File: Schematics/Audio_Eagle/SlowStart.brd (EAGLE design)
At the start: 100 x 80 mm, 19 parts

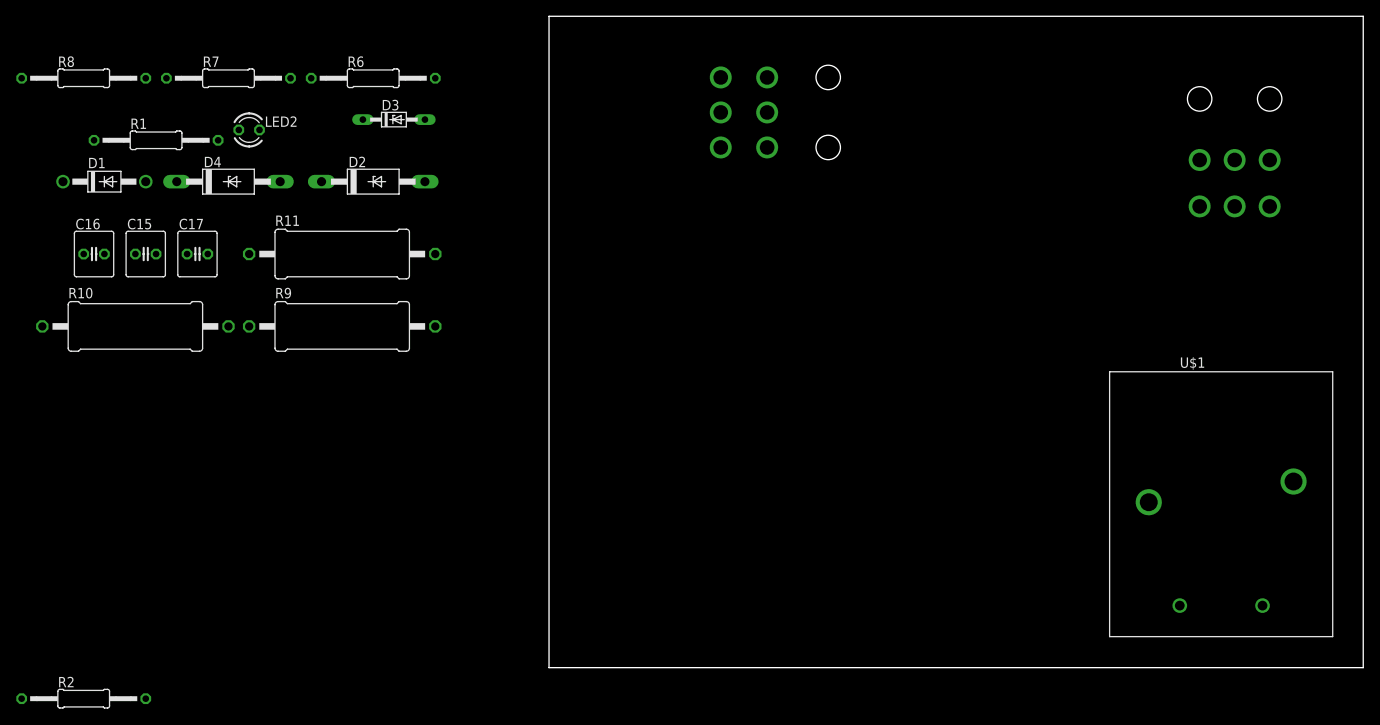
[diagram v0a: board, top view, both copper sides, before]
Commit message: updated slow start
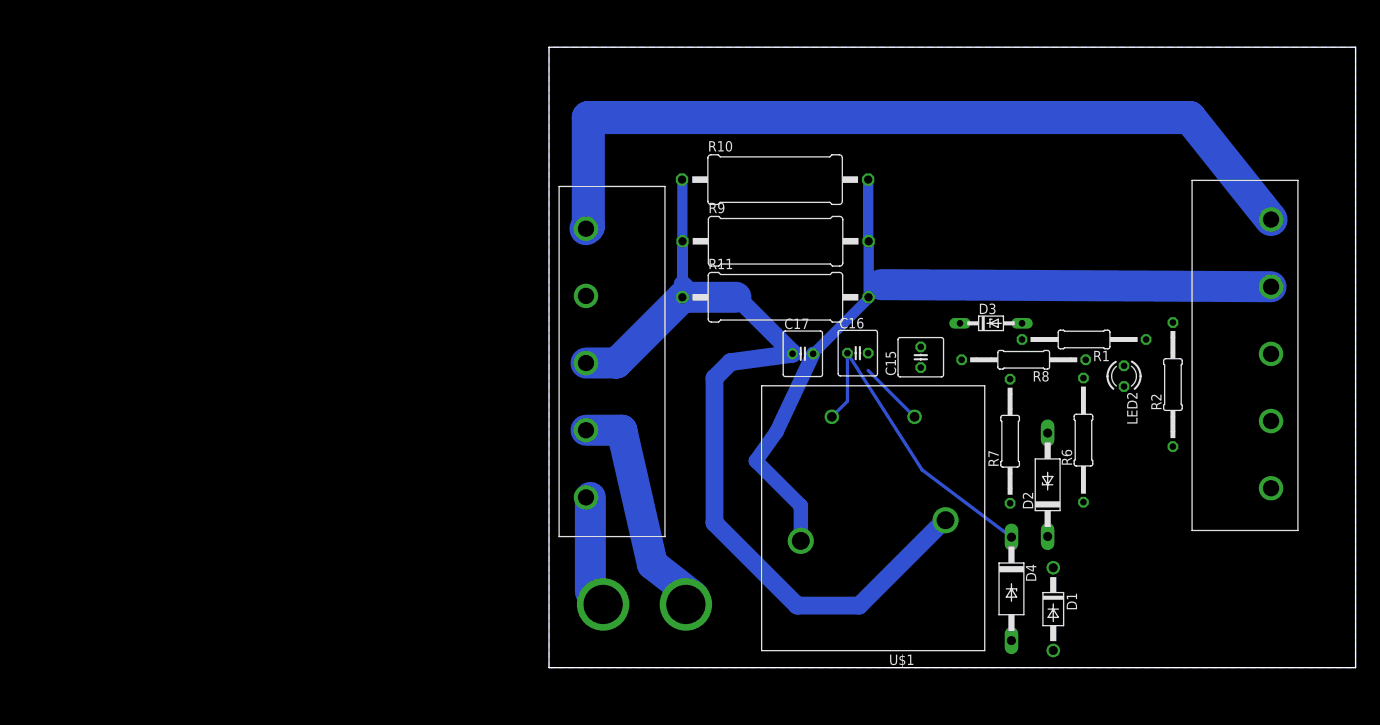
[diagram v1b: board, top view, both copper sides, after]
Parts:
- added U$4: FUSE, Amplifier_Parts:FUSE_PADS
- U$2, U$3: value MOLEX_6P -> SCREW_TERMINAL_5; device Amplifier_Parts:MOLEX_6P -> Amplifier_Parts:SCREW_TERMINAL_5
- moved R2 139.2 mm to (76.6, 34.8), turned to 90 degrees
- moved D1 127.8 mm to (61.9, 7.19), turned to 270 degrees
- moved R8 120.5 mm to (58.3, 37.8), turned to 180 degrees
- moved R1 116.6 mm to (65.7, 40.3), turned to 180 degrees
- moved LED2 111.6 mm to (70.6, 35.8), turned to 270 degrees
- moved D4 108.4 mm to (56.8, 9.68), turned to 270 degrees
- moved R7 105.8 mm to (56.6, 27.8), turned to 90 degrees
- moved R6 97.9 mm to (65.6, 27.9), turned to 90 degrees
- moved C15 96.0 mm to (45.7, 38.1), turned to 90 degrees
- moved C16 94.6 mm to (37.9, 38.6)
- moved D2 90.8 mm to (61.2, 22.5), turned to 90 degrees
- moved U$2 88.0 mm to (2.54, 38.1), turned to 270 degrees
- moved R10 80.6 mm to (27.8, 59.9)
- moved D3 77.5 mm to (54.3, 42.3)
- moved C17 75.4 mm to (31.2, 38.5)
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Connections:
- removed net N$1 (its old number): U$2.P$3, U$2.P$4
- new net VAC+: U$2.P$4, U$3.P$6
- new net VAC-: C17.1, R10.1, R11.1, R9.1, U$1.COM, U$2.P$3
- net GND: now also U$2.P$2; no longer U$2.P$1
- net N$12: now also U$3.P$4; no longer U$3.P$5
- net N$2: now also U$2.P$6, U$4.P$2; no longer U$2.P$5, U$3.P$3
- net N$3: now also R2.2, U$3.P$3; no longer C17.1, R10.1, R11.1, R9.1, U$1.COM, U$2.P$2
- net N$5: now also U$2.P$5, U$4.P$1; no longer R2.2, U$3.P$2
- net N$8: now also U$3.P$5; no longer U$3.P$4
- net VCC: no longer U$3.P$1
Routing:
- net VAC-: track 0.00 -> 133.6 mm
- net VAC+: track 0.00 -> 103.7 mm
- net N$8: track 0.00 -> 101.4 mm
- net N$10: track 0.00 -> 39.4 mm
- net N$5: track 0.00 -> 29.1 mm
- net N$2: track 0.00 -> 14.3 mm
- net GND: track 0.00 -> 8.06 mm
- added copper zone on layer 16, net GND
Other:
- board size 100 x 80 mm -> 99.1 x 76.2 mm

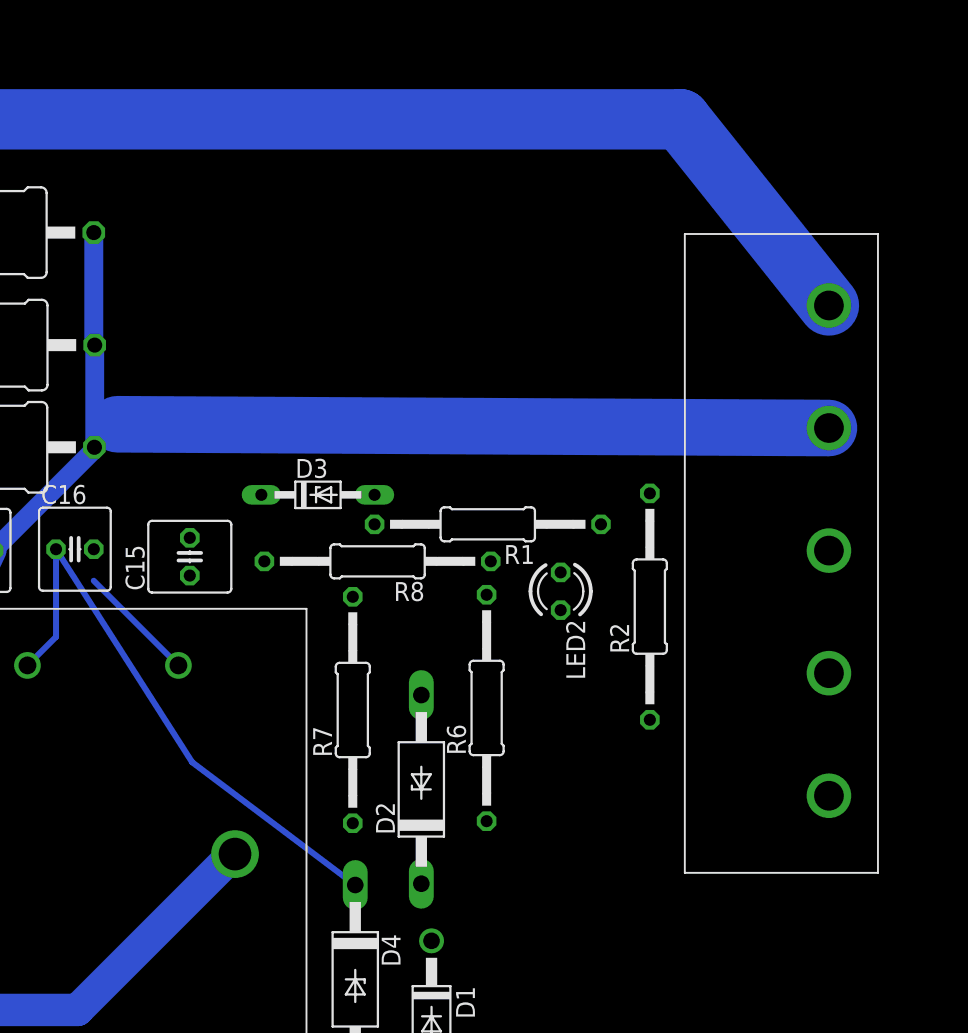
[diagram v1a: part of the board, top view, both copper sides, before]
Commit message: updated to slow start board
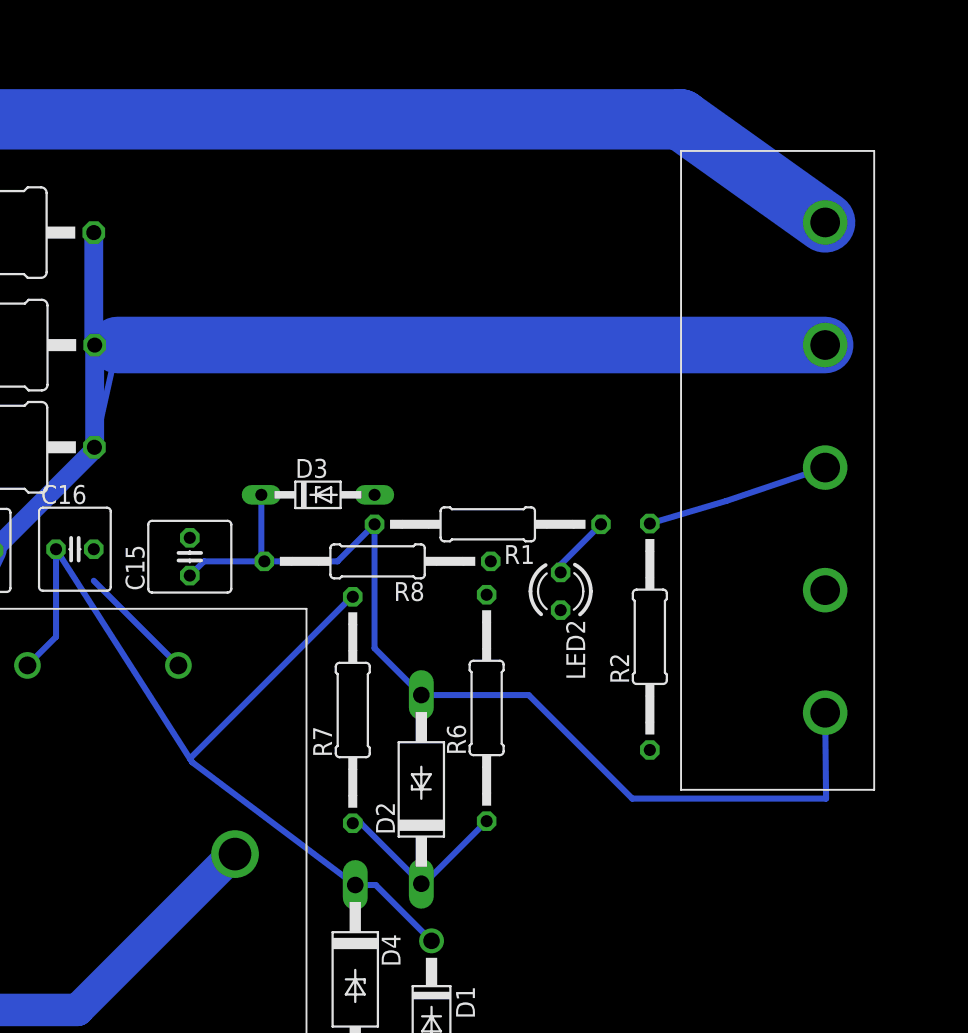
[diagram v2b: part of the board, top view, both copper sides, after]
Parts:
- moved U$3 5.59 mm to (90.4, 43.4)
- moved R2 2.03 mm to (76.6, 32.7)
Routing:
- net N$12: track 0.00 -> 67.1 mm
- net N$10: track 39.4 -> 61.5 mm
- net N$11: track 0.00 -> 12.4 mm
- net N$3: track 0.00 -> 12.4 mm
- net N$8: track 101.4 -> 106.0 mm
- net N$1: track 0.00 -> 4.36 mm
- net VAC+: track 103.7 -> 99.6 mm
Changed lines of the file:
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@@
 </element>
 <element name="R1" library="resistor" package="0207/15" value="10k" x="65.7141" y="40.3049625" rot="R180"/>
-<element name="R2" library="resistor" package="0207/15" value="100" x="76.623821875" y="34.768103125" rot="R90"/>
+<element name="R2" library="resistor" package="0207/15" value="100" x="76.623821875" y="32.736103125" rot="R90"/>
 <element name="U$4" library="Amplifier_Parts" package="FUSE_PADS" value="FUSE" x="11.7266" y="7.763428125" rot="R180"/>
 <element name="U$2" library="Amplifier_Parts" package="SCREW_TERMINAL_5" value="SCREW_TERMINAL_5" x="2.54" y="38.1" rot="R270"/>
-<element name="U$3" library="Amplifier_Parts" package="SCREW_TERMINAL_5" value="SCREW_TERMINAL_5" x="90.678" y="37.846" rot="R90"/>
+<element name="U$3" library="Amplifier_Parts" package="SCREW_TERMINAL_5" value="SCREW_TERMINAL_5" x="90.424" y="43.434" rot="R90"/>
 </elements>
 <signals>
@@
 <wire x1="39.23845" y1="45.489928125" x2="39.23845" y2="45.34414375" width="1.27" layer="16"/>
 <wire x1="39.23845" y1="45.34414375" x2="32.4429" y2="38.54859375" width="1.27" layer="16"/>
-<wire x1="39.257265625" y1="45.50874375" x2="40.788521875" y2="47.04" width="0.4064" layer="16"/>
-<wire x1="40.788521875" y1="47.04" x2="88.678" y2="46.786" width="3.81" layer="16"/>
+<wire x1="39.257265625" y1="45.50874375" x2="40.788521875" y2="52.374" width="0.4064" layer="16"/>
+<wire x1="40.788521875" y1="52.374" x2="88.424" y2="52.374" width="3.81" layer="16"/>
 </signal>
 <signal name="N$10">
@@
 <wire x1="56.795371875" y1="16.027840625" x2="45.820628125" y2="24.288884375" width="0.4064" layer="16"/>
 <wire x1="45.820628125" y1="24.288884375" x2="36.65525625" y2="38.629" width="0.4064" layer="16"/>
-<wire x1="45.820628125" y1="24.288884375" x2="56.6285875" y2="35.426621875" width="0" layer="19" extent="16-16"/>
-<wire x1="61.9296125" y1="12.269978125" x2="56.795371875" y2="16.027840625" width="0" layer="19" extent="1-1"/>
+<wire x1="56.6285875" y1="35.426621875" x2="56.55949375" y2="35.426621875" width="0.4064" layer="16"/>
+<wire x1="56.55949375" y1="35.426621875" x2="45.665096875" y2="24.532225" width="0.4064" layer="16"/>
+<wire x1="56.795371875" y1="16.027840625" x2="58.17175" y2="16.027840625" width="0.4064" layer="16"/>
+<wire x1="58.17175" y1="16.027840625" x2="61.9296125" y2="12.269978125" width="0.4064" layer="16"/>
+<wire x1="45.820628125" y1="24.288884375" x2="45.665096875" y2="24.532225" width="0" layer="19" extent="16-16"/>
 </signal>
 <signal name="N$11">
@@
 <contactref element="R6" pad="1"/>
 <contactref element="D2" pad="C"/>
-<wire x1="61.242603125" y1="16.113271875" x2="65.637840625" y2="20.324825" width="0" layer="19" extent="1-1"/>
-<wire x1="56.6285875" y1="20.186621875" x2="61.242603125" y2="16.113271875" width="0" layer="19" extent="1-1"/>
+<wire x1="56.6285875" y1="20.186621875" x2="57.169253125" y2="20.186621875" width="0.4064" layer="16"/>
+<wire x1="57.169253125" y1="20.186621875" x2="61.242603125" y2="16.113271875" width="0.4064" layer="16"/>
+<wire x1="61.242603125" y1="16.113271875" x2="61.4262875" y2="16.113271875" width="0.4064" layer="16"/>
+<wire x1="61.4262875" y1="16.113271875" x2="65.637840625" y2="20.324825" width="0.4064" layer="16"/>
 </signal>
 <signal name="N$12">
@@
 <contactref element="R1" pad="2"/>
 <contactref element="U$3" pad="P$4"/>
-<wire x1="61.242603125" y1="28.813271875" x2="88.678" y2="22.036" width="0" layer="19" extent="1-1"/>
-<wire x1="58.0941" y1="40.3049625" x2="61.242603125" y2="28.813271875" width="0" layer="19" extent="1-1"/>
-<wire x1="50.677503125" y1="37.812834375" x2="58.0941" y2="40.3049625" width="0" layer="19" extent="1-1"/>
-<wire x1="50.47415" y1="42.289403125" x2="50.677503125" y2="37.812834375" width="0" layer="19" extent="1-1"/>
-<wire x1="45.658725" y1="36.85528125" x2="50.677503125" y2="37.812834375" width="0" layer="19" extent="1-1"/>
+<wire x1="50.677503125" y1="37.812834375" x2="46.616278125" y2="37.812834375" width="0.4064" layer="16"/>
+<wire x1="46.616278125" y1="37.812834375" x2="45.658725" y2="36.85528125" width="0.4064" layer="16"/>
+<wire x1="50.47415" y1="42.289403125" x2="50.47415" y2="38.0161875" width="0.4064" layer="16"/>
+<wire x1="50.47415" y1="38.0161875" x2="50.677503125" y2="37.812834375" width="0.4064" layer="16"/>
+<wire x1="50.677503125" y1="37.812834375" x2="55.601971875" y2="37.812834375" width="0.4064" layer="16"/>
+<wire x1="55.601971875" y1="37.812834375" x2="58.0941" y2="40.3049625" width="0.4064" layer="16"/>
+<wire x1="58.0941" y1="40.3049625" x2="58.0941" y2="31.961775" width="0.4064" layer="16"/>
+<wire x1="58.0941" y1="31.961775" x2="61.242603125" y2="28.813271875" width="0.4064" layer="16"/>
+<wire x1="61.242603125" y1="28.813271875" x2="68.468728125" y2="28.813271875" width="0.4064" layer="16"/>
+<wire x1="68.468728125" y1="28.813271875" x2="75.438" y2="21.844" width="0.4064" layer="16"/>
+<wire x1="75.438" y1="21.844" x2="88.486" y2="21.844" width="0.4064" layer="16"/>
+<wire x1="88.486" y1="21.844" x2="88.424" y2="27.624" width="0.4064" layer="16"/>
 </signal>
 <signal name="VAC+">
@@
 <wire x1="4.826" y1="54.196" x2="4.826" y2="67.564" width="4.064" layer="16"/>
 <wire x1="4.826" y1="67.564" x2="78.69" y2="67.564" width="4.064" layer="16"/>
-<wire x1="78.69" y1="67.564" x2="88.678" y2="55.036" width="4.064" layer="16"/>
+<wire x1="78.69" y1="67.564" x2="88.424" y2="60.624" width="4.064" layer="16"/>
 </signal>
 <signal name="N$2">
@@
 <contactref element="LED2" pad="A"/>
 <contactref element="R1" pad="1"/>
-<wire x1="70.620678125" y1="37.068765625" x2="73.3341" y2="40.3049625" width="0" layer="19" extent="1-1"/>
+<wire x1="70.620678125" y1="37.068765625" x2="70.620678125" y2="37.591540625" width="0.4064" layer="16"/>
+<wire x1="70.620678125" y1="37.591540625" x2="73.3341" y2="40.3049625" width="0.4064" layer="16"/>
 </signal>
 <signal name="N$3">
 <contactref element="R2" pad="2"/>
 <contactref element="U$3" pad="P$3"/>
-<wire x1="76.623821875" y1="42.388103125" x2="88.678" y2="38.536" width="0" layer="19" extent="1-1"/>
+<wire x1="76.623821875" y1="40.356103125" x2="81.777896875" y2="41.880103125" width="0.4064" layer="16"/>
+<wire x1="81.777896875" y1="41.880103125" x2="88.424" y2="44.124" width="0.4064" layer="16"/>
 </signal>
 </signals>

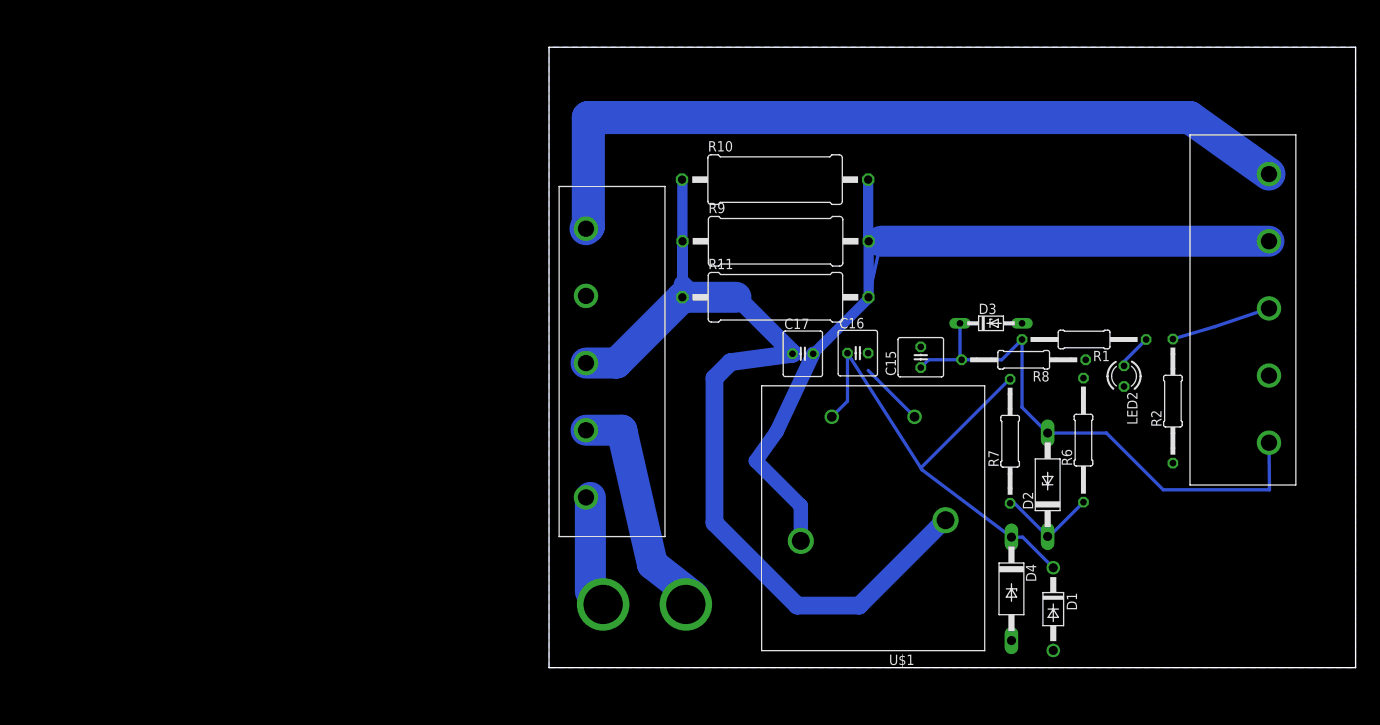
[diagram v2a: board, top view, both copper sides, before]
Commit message: changes to slow start
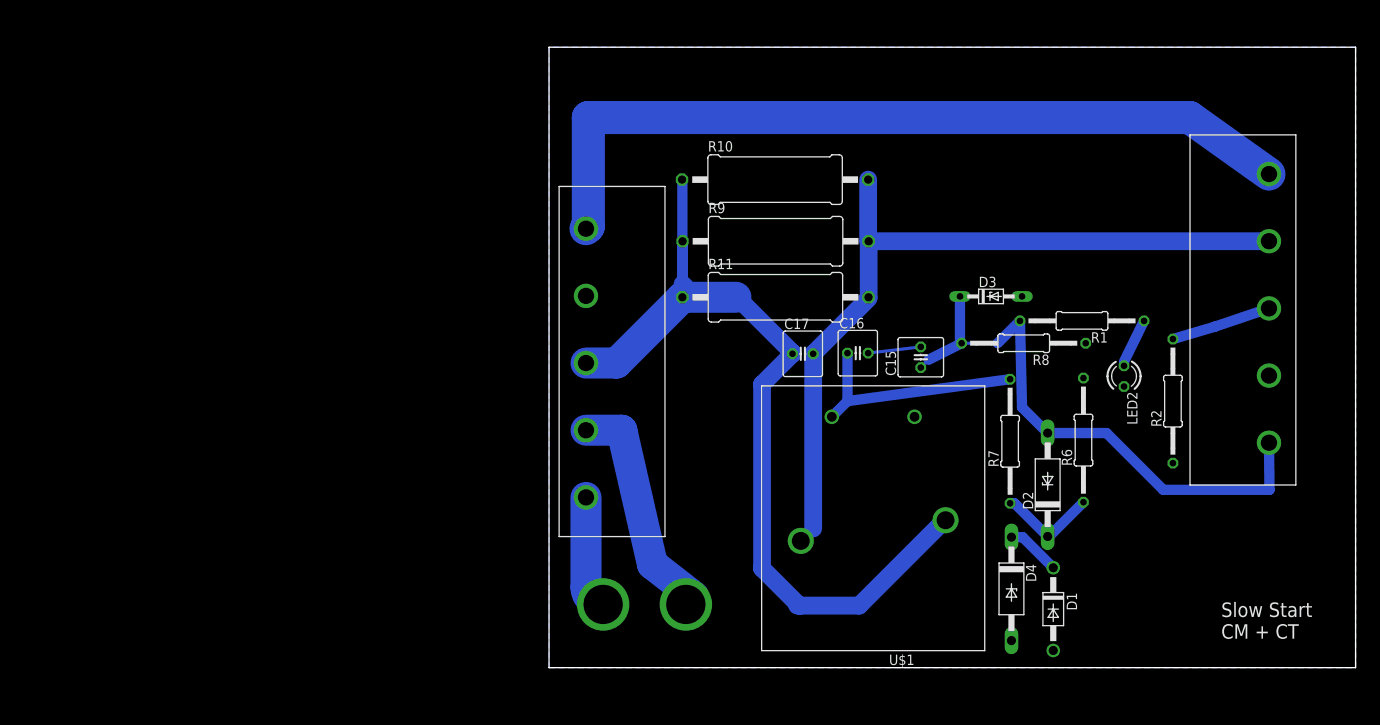
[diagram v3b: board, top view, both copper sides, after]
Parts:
- moved D3 3.30 mm to (54.3, 45.6)
- moved R1 2.30 mm to (65.5, 42.6)
- moved R8 2.03 mm to (58.3, 39.8)
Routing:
- net N$10: track 61.5 -> 35.5 mm
- net N$8: track 106.0 -> 97.0 mm
- net VAC-: track 133.6 -> 125.4 mm
- net N$12: track 67.1 -> 71.0 mm
- net N$1: track 4.36 -> 6.09 mm
- net GND: track 8.06 -> 6.51 mm
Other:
- board text added: "Slow Start CM + CT"
